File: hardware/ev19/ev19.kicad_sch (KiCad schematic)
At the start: 164 parts, among them CN1 Conn_05x02_Female, J1 USB_C_Receptacle, J11 Conn_02x05_Counter_Clockwise, J13 USB_C_Receptacle_USB2.0_16P, J2 Conn_01x02_Socket, J4 Conn_02x03_Odd_Even, J5 Conn_02x03_Odd_Even, J6 Conn_02x05_Counter_Clockwise, J7 Conn_02x05_Counter_Clockwise, J8 Conn_02x05_Counter_Clockwise, J9 Conn_02x05_Counter_Clockwise, Q1 2N7002, Q2 2N7002, Q3 2N7002, Q4 2N7002, SW1 SW_SPDT, SW2 SW_Push, SW3 SW_Push, U1 BQ21040DBV, U12 XC6227C301MR-G, U2 USBLC6-2P6, U3 STM32F072CBTx, U4 CH340C, U5 TPS63060, U7 ESP32-S3-WROOM-1, U9 TPS2116DRL, Y1 Crystal_GND24

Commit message: wip- laid out the analog power section, added screen cut outs, decided on positions
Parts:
- removed H5: MountingHole, MountingHole:MountingHole_2.7mm_M2.5, symbol Mechanical:MountingHole
- removed J13: USB_C_Receptacle_USB2.0_16P, Connector_USB:USB_C_Receptacle_HRO_TYPE-C-31-M-12, symbol Connector:USB_C_Receptacle_USB2.0_16P
- added J10: USB_C_Receptacle, Connector_USB:USB_C_Receptacle_HRO_TYPE-C-31-M-12, symbol Connector:USB_C_Receptacle_USB2.0_16P
- JP1: footprint Jumper:SolderJumper-3_P1.3mm_Bridged12_RoundedPad1.0x1.5mm -> (none)
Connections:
- net UI_SCL1: no longer R16.2
- net UI_SDA1: no longer R19.2
- net +3.3V_ES8311 renamed +3.3V_WM8960
- net ES8311_Sense renamed WM8960_Sense
- new net: J10.A1 (GND), J10.A12 (GND), J10.B1 (GND), J10.B12 (GND)
- new net: J10.A4 (VBUS), J10.A9 (VBUS), J10.B4 (VBUS), J10.B9 (VBUS)
- new net I2C1_SCL: R19.2
- new net I2C1_SDA: R16.2
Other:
- note removed: "7.071"
- moved on the sheet: C10, C11, C18, C7, JP3, NT1, R2, R52, U12

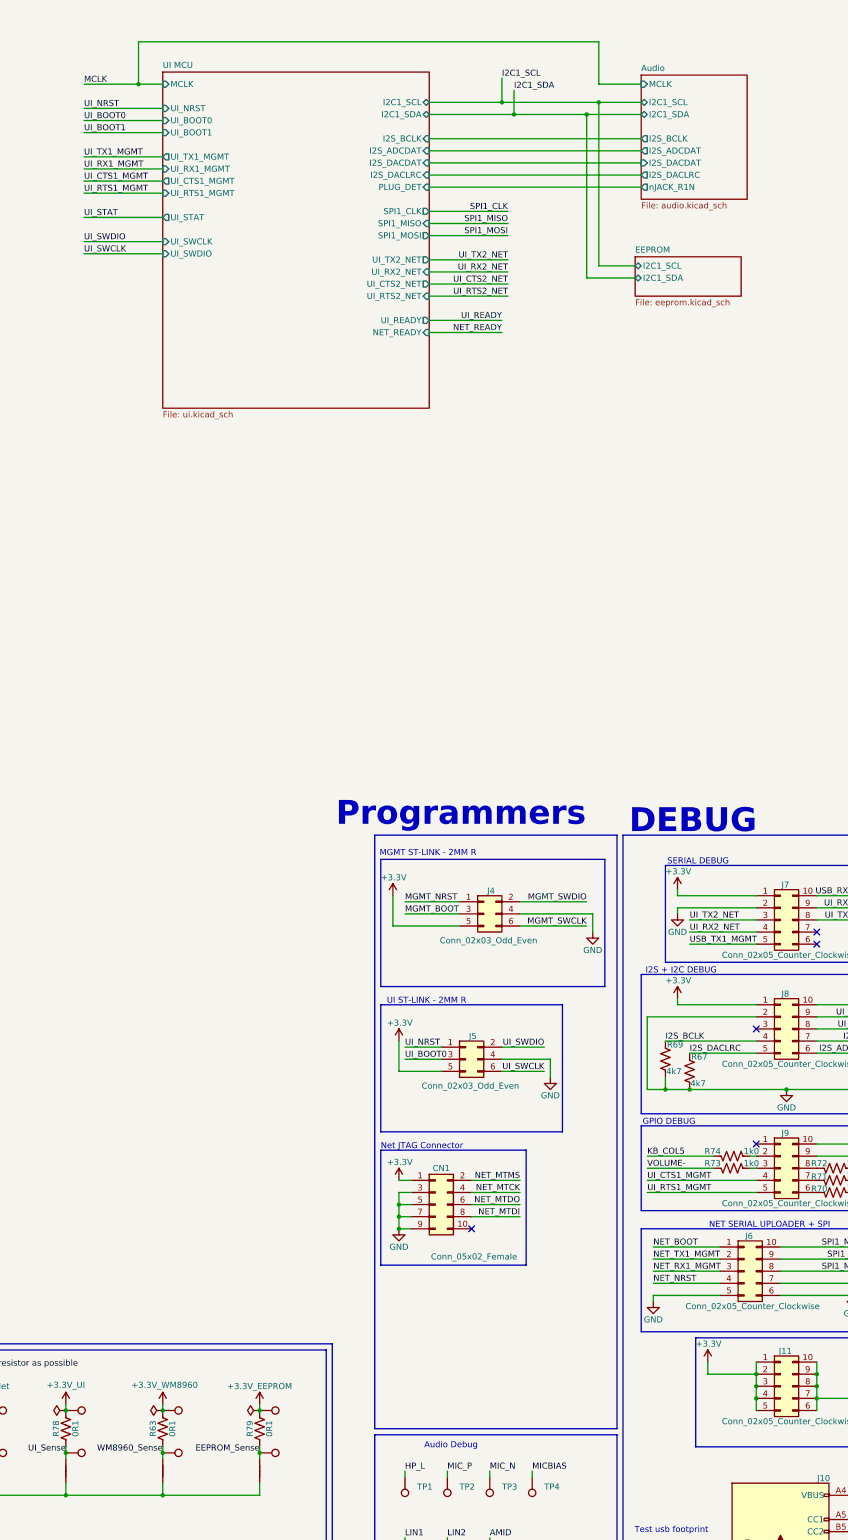
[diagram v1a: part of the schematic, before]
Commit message: Laid out all high speed lines, created gnda, 3.0va, and dgnd 3.3vd in analog sections
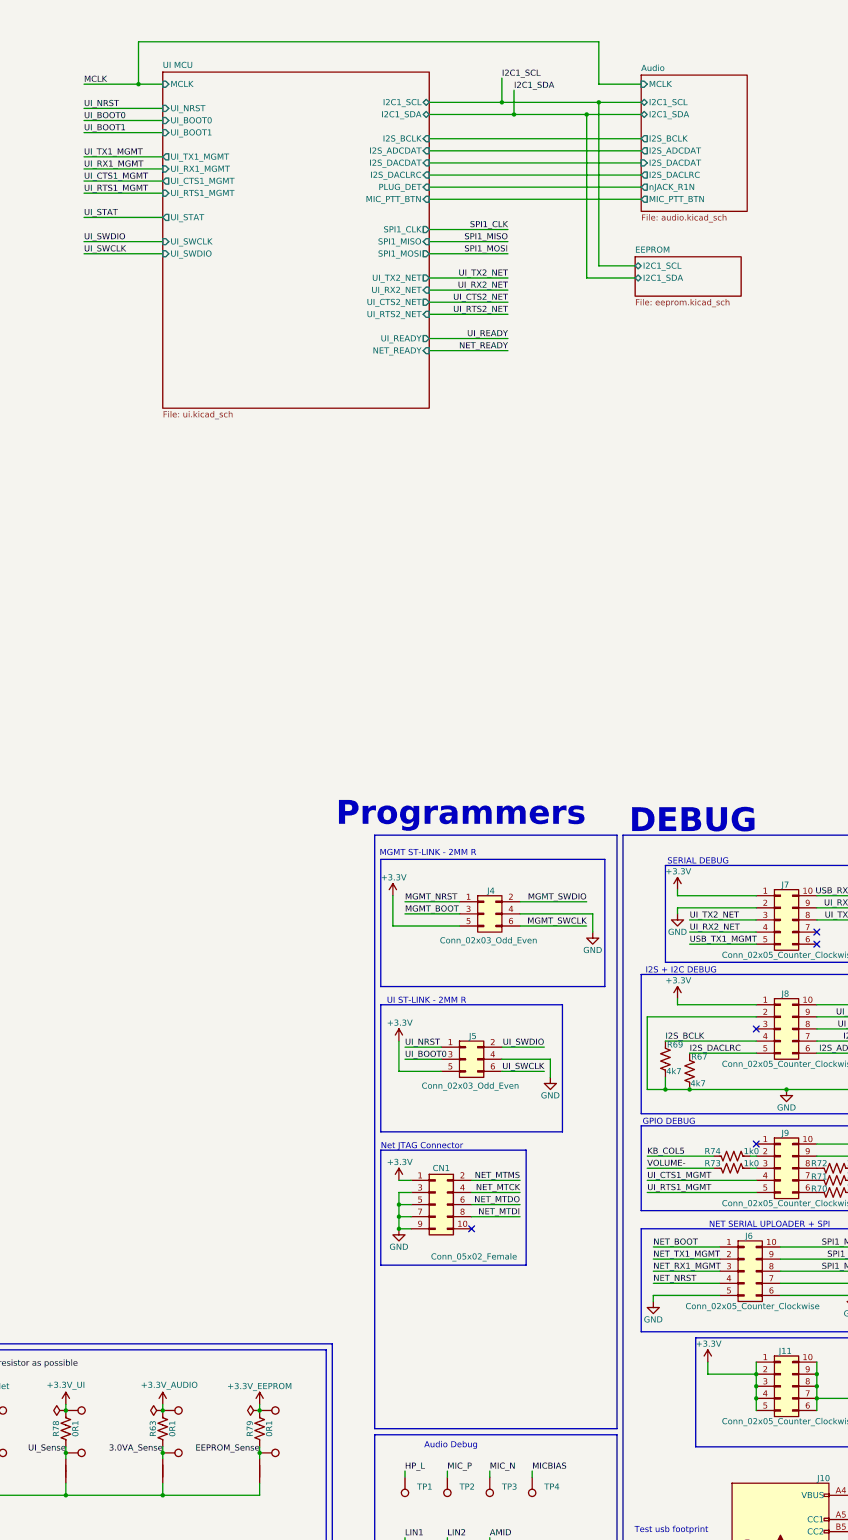
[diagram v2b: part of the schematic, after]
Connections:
- net +3.3V_WM8960 renamed +3.3V_AUDIO
- net WM8960_Sense renamed 3.0VA_Sense
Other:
- sheet Audio ports: added MIC_PTT_BTN; removed none
- sheet UI MCU ports: added MIC_PTT_BTN; removed none
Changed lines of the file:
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@@
 	(wire
 		(pts
-			(xy 482.6 63.5) (xy 466.09 63.5)
+			(xy 482.6 67.31) (xy 466.09 67.31)
 		)
 		(stroke
@@
 	(wire
 		(pts
-			(xy 482.6 60.96) (xy 466.09 60.96)
+			(xy 482.6 64.77) (xy 466.09 64.77)
 		)
 		(stroke
@@
 	(wire
 		(pts
-			(xy 466.09 83.82) (xy 481.33 83.82)
+			(xy 466.09 87.63) (xy 482.6 87.63)
 		)
 		(stroke
@@
 	(wire
 		(pts
-			(xy 466.09 73.66) (xy 482.6 73.66)
+			(xy 466.09 77.47) (xy 482.6 77.47)
 		)
 		(stroke
@@
 	(wire
 		(pts
-			(xy 466.09 78.74) (xy 482.6 78.74)
+			(xy 466.09 82.55) (xy 482.6 82.55)
 		)
 		(stroke
@@
 	(wire
 		(pts
-			(xy 466.09 76.2) (xy 482.6 76.2)
+			(xy 466.09 80.01) (xy 482.6 80.01)
 		)
 		(stroke
@@
 	(wire
 		(pts
-			(xy 466.09 71.12) (xy 482.6 71.12)
+			(xy 466.09 74.93) (xy 482.6 74.93)
 		)
 		(stroke
@@
 	(wire
 		(pts
+			(xy 466.09 58.42) (xy 510.54 58.42)
+		)
+		(stroke
+			(width 0)
+			(type default)
+		)
+	)
+	(wire
+		(pts
 			(xy 199.39 342.9) (xy 199.39 341.63)
 		)
@@
 	(wire
 		(pts
-			(xy 466.09 86.36) (xy 481.33 86.36)
+			(xy 466.09 90.17) (xy 482.6 90.17)
 		)
 		(stroke
@@
 	(wire
 		(pts
-			(xy 482.6 66.04) (xy 466.09 66.04)
+			(xy 482.6 69.85) (xy 466.09 69.85)
 		)
 		(stroke
@@
 	)
 	(label "UI_RTS2_NET"
-		(at 482.6 78.74 180)
+		(at 482.6 82.55 180)
 		(effects
 			(font
@@
 	)
 	(label "SPI1_CLK"
-		(at 482.6 60.96 180)
+		(at 482.6 64.77 180)
 		(effects
 			(font
@@
 	)
 	(label "UI_CTS2_NET"
-		(at 482.6 76.2 180)
+		(at 482.6 80.01 180)
 		(effects
 			(font
@@
 	)
 	(label "SPI1_MISO"
-		(at 482.6 63.5 180)
+		(at 482.6 67.31 180)
 		(effects
 			(font
@@
 	)
 	(label "UI_RX2_NET"
-		(at 482.6 73.66 180)
+		(at 482.6 77.47 180)
 		(effects
 			(font
@@
 	)
 	(label "NET_READY"
-		(at 481.33 86.36 180)
+		(at 482.6 90.17 180)
 		(effects
 			(font
@@
 		)
 	)
-	(label "WM8960_Sense"
+	(label "3.0VA_Sense"
 		(at 410.21 321.31 180)
 		(effects
@@
 	)
 	(label "UI_READY"
-		(at 481.33 83.82 180)
+		(at 482.6 87.63 180)
 		(effects
 			(font
@@
 	)
 	(label "UI_TX2_NET"
-		(at 482.6 71.12 180)
+		(at 482.6 74.93 180)
 		(effects
 			(font
@@
 	)
 	(label "SPI1_MOSI"
-		(at 482.6 66.04 180)
+		(at 482.6 69.85 180)
 		(effects
 			(font
@@
 			)
 		)
-		(property "Value" "+3.3V_WM8960"
+		(property "Value" "+3.3V_AUDIO"
 			(at 417.576 307.086 0)
 			(show_name no)
@@
 		)
 		(pin "NET_READY" input
-			(at 466.09 86.36 0)
+			(at 466.09 90.17 0)
 			(effects
 				(font
@@
 		)
 		(pin "SPI1_CLK" output
-			(at 466.09 60.96 0)
+			(at 466.09 64.77 0)
 			(effects
 				(font
@@
 		)
 		(pin "SPI1_MOSI" output
-			(at 466.09 66.04 0)
+			(at 466.09 69.85 0)
 			(effects
 				(font
@@
 		)
 		(pin "UI_CTS2_NET" output
-			(at 466.09 76.2 0)
+			(at 466.09 80.01 0)
 			(effects
 				(font
@@
 		)
 		(pin "UI_READY" output
-			(at 466.09 83.82 0)
+			(at 466.09 87.63 0)
 			(effects
 				(font
@@
 		)
 		(pin "UI_RTS2_NET" input
-			(at 466.09 78.74 0)
+			(at 466.09 82.55 0)
 			(effects
 				(font
@@
 		)
 		(pin "UI_RX2_NET" input
-			(at 466.09 73.66 0)
+			(at 466.09 77.47 0)
 			(effects
 				(font
@@
 		)
 		(pin "UI_TX2_NET" output
-			(at 466.09 71.12 0)
+			(at 466.09 74.93 0)
 			(effects
 				(font
@@
 		)
 		(pin "SPI1_MISO" input
-			(at 466.09 63.5 0)
+			(at 466.09 67.31 0)
 			(effects
 				(font
@@
 			)
 		)
+		(pin "MIC_PTT_BTN" input
+			(at 466.09 58.42 0)
+			(effects
+				(font
+					(size 1.27 1.27)
+				)
+				(justify right)
+			)
+		)
 		(instances
 			(project "ev19"
@@
 	(sheet
 		(at 510.54 32.385)
-		(size 22.225 26.035)
+		(size 22.225 28.575)
 		(exclude_from_sim no)
 		(in_bom yes)
@@
 		)
 		(property "Sheetfile" "audio.kicad_sch"
-			(at 510.54 59.0046 0)
+			(at 510.54 61.5446 0)
 			(show_name no)
 			(do_not_autoplace no)
@@
 			(effects
 				(font
+					(size 1.27 1.27)
+				)
+				(justify left)
+			)
+		)
+		(pin "MIC_PTT_BTN" output
+			(at 510.54 58.42 180)
+			(effects
+				(font

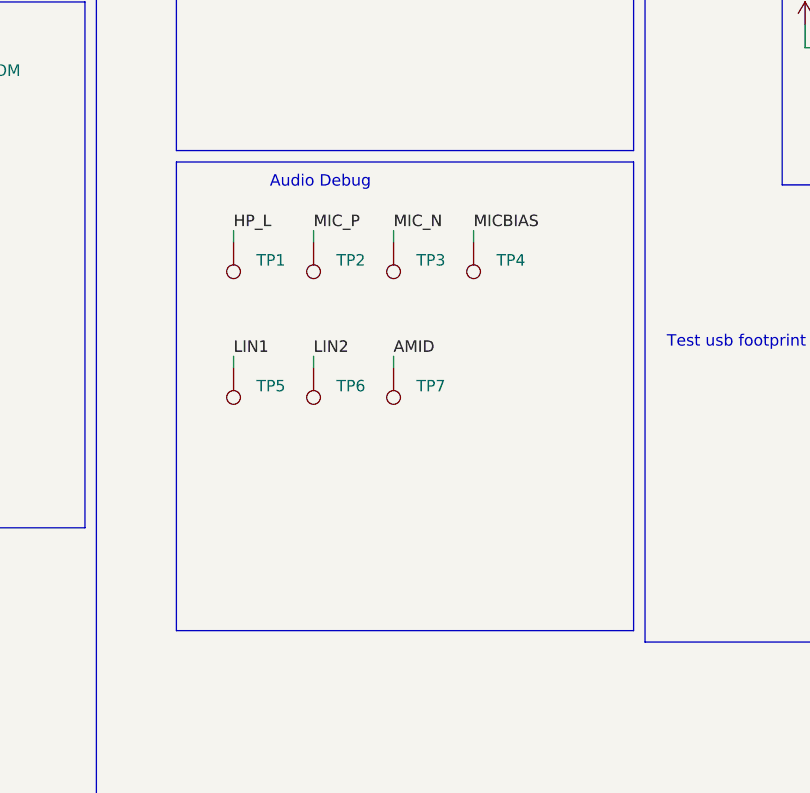
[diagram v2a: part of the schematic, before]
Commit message: Fixed ES8311 symbol, pins were wrong. Laid out audio section. Routed many non-high speed traces
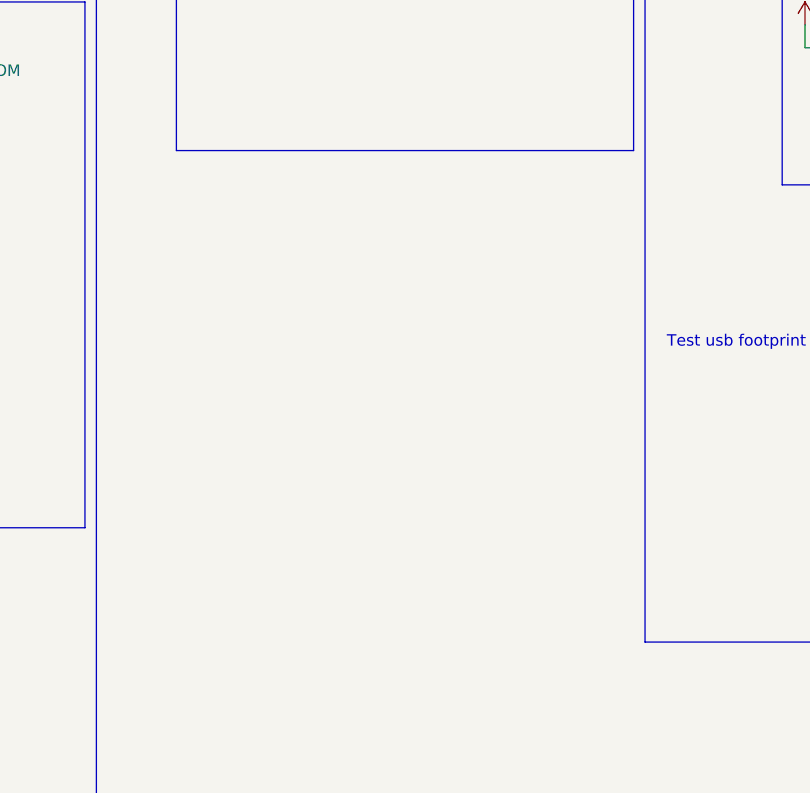
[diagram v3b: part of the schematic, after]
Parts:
- removed TP1, TP2, TP3, TP4, TP5, TP6, TP7: TestPoint, TestPoint:TestPoint_THTPad_D2.0mm_Drill1.0mm, symbol Connector:TestPoint
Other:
- note removed: "Audio Debug"

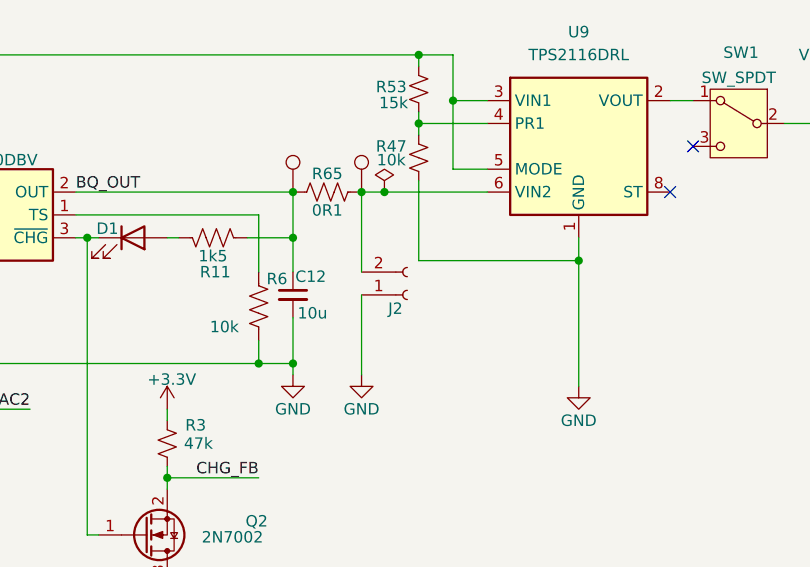
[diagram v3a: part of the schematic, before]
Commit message: Redesigned digital section again to fit the battery better. Chose where the screen connector and battery connector go
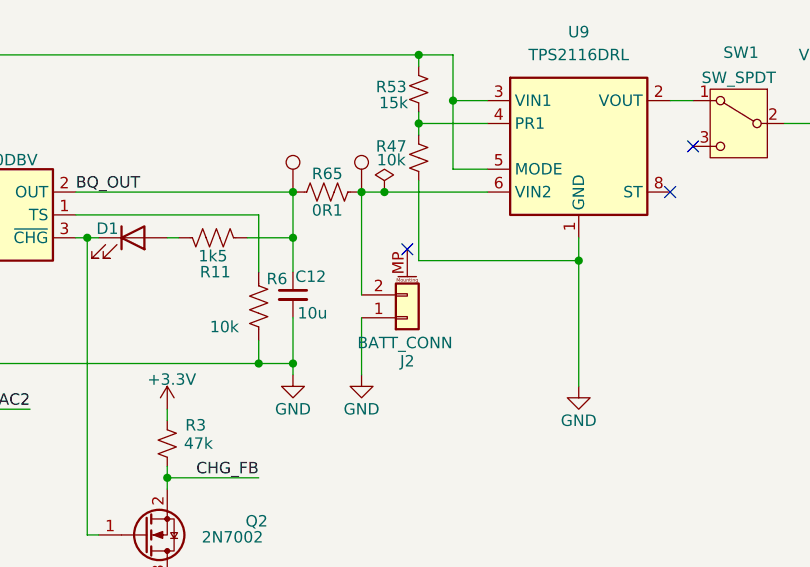
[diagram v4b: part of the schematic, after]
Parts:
- removed J2: Conn_01x02_Socket, Hactar_Footprints:JST_PH_S2B-PH-SM4-TB_1x02-1MP_P2.00mm_Horizontal, symbol Connector:Conn_01x02_Socket
- added J2: BATT_CONN, Connector_JST:JST_PH_S2B-PH-SM4-TB_1x02-1MP_P2.00mm_Horizontal, symbol Connector_Generic_MountingPin:Conn_01x02_MountingPin
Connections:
- net GND: now also J2.1 (Pin_1)
- net at R65.2, TP32.1, U9.6 (VIN2): now also J2.2 (Pin_2)
- no-connect marks 41 -> 42
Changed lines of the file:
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@@
 	)
 	(no_connect
+		(at 92.71 342.9)
+	)
+	(no_connect
 		(at 532.13 368.3)
 	)
@@
 	(wire
 		(pts
-			(xy 87.63 347.98) (xy 87.63 356.87)
+			(xy 87.63 350.52) (xy 87.63 356.87)
 		)
 		(stroke
@@
 	(wire
 		(pts
-			(xy 87.63 336.55) (xy 87.63 345.44)
+			(xy 87.63 336.55) (xy 87.63 347.98)
 		)
 		(stroke
@@
 	)
 	(symbol
+		(lib_id "Connector_Generic_MountingPin:Conn_01x02_MountingPin")
+		(at 92.71 350.52 0)
+		(mirror x)
+		(unit 1)
+		(body_style 1)
+		(exclude_from_sim no)
+		(in_bom yes)
+		(on_board yes)
+		(in_pos_files yes)
+		(dnp no)
+		(property "Reference" "J2"
+			(at 92.71 355.346 0)
+			(show_name no)
+			(do_not_autoplace no)
+			(effects
+				(font
+					(size 1.27 1.27)
+				)
+			)
+		)
+		(property "Value" "BATT_CONN"
+			(at 92.456 353.314 0)
+			(show_name no)
+			(do_not_autoplace no)
+			(effects
+				(font
+					(size 1.27 1.27)
+				)
+			)
+		)
+		(property "Footprint" "Connector_JST:JST_PH_S2B-PH-SM4-TB_1x02-1MP_P2.00mm_Horizontal"
+			(at 92.71 350.52 0)
+			(hide yes)
+			(show_name no)
+			(do_not_autoplace no)
+			(effects
+				(font
+					(size 1.27 1.27)
+				)
+			)
+		)
+		(property "Datasheet" ""
+			(at 92.71 350.52 0)
+			(hide yes)
+			(show_name no)
+			(do_not_autoplace no)
+			(effects
+				(font
+					(size 1.27 1.27)
+				)
+			)
+		)
+		(property "Description" "Generic connectable mounting pin connector, single row, 01x02, script generated (kicad-library-utils/schlib/autogen/connector/)"
+			(at 92.71 350.52 0)
+			(hide yes)
+			(show_name no)
+			(do_not_autoplace no)
+			(effects
+				(font
+					(size 1.27 1.27)
+				)
+			)
+		)
+		(property "JLCPCB Part #" "C295747"
+			(at 92.71 350.52 0)
+			(hide yes)
+			(show_name no)
+			(do_not_autoplace no)
+			(effects
+				(font
+					(size 1.27 1.27)
+				)
+			)
+		)
+		(pin "1"
+		)
+		(pin "2"
+		)
+		(pin "MP"
+		)
+		(instances
+			(project "ev19"
+				(path "/bd865368-262b-4f76-b7a6-1673c2cb0f8c"
+					(reference "J2")
+					(unit 1)
+				)
+			)
+		)
+	)
+	(symbol
 		(lib_id "Device:C_Small")
 		(at 187.96 345.44 0)
@@
 					(unit 1)
 				)
-			)
-		)
-	)
-	(symbol
-		(lib_id "Connector:Conn_01x02_Socket")
-		(at 92.71 347.98 0)
-		(mirror x)
-		(unit 1)
-		(body_style 1)
-		(exclude_from_sim no)
-		(in_bom yes)
-		(on_board yes)
-		(in_pos_files yes)
-		(dnp no)
-		(property "Reference" "J2"
-			(at 92.202 349.504 0)
-			(show_name no)
-			(do_not_autoplace no)
-			(effects
-				(font
-					(size 1.27 1.27)
-				)
-				(justify right)
-			)
-		)
-		(property "Value" "Conn_01x02_Socket"
-			(at 96.52 354.33 90)
-			(hide yes)
-			(show_name no)
-			(do_not_autoplace no)
-			(effects
-				(font
-					(size 1.27 1.27)
-				)
-				(justify right)
-			)
-		)
-		(property "Footprint" "Hactar_Footprints:JST_PH_S2B-PH-SM4-TB_1x02-1MP_P2.00mm_Horizontal"
-			(at 92.71 347.98 0)
-			(hide yes)
-			(show_name no)
-			(do_not_autoplace no)
-			(effects
-				(font
-					(size 1.27 1.27)
-				)
-			)
-		)
-		(property "Datasheet" ""
-			(at 92.71 347.98 0)
-			(hide yes)
-			(show_name no)
-			(do_not_autoplace no)
-			(effects
-				(font
-					(size 1.27 1.27)
-				)
-			)
-		)
-		(property "Description" "Generic connector, single row, 01x02, script generated"
-			(at 92.71 347.98 0)
-			(hide yes)
-			(show_name no)
-			(do_not_autoplace no)
-			(effects
-				(font
-					(size 1.27 1.27)
-				)
-			)
-		)
-		(property "JLCPCB Part #" "C295747"
-			(at 92.71 347.98 0)
-			(hide yes)
-			(show_name no)
-			(do_not_autoplace no)
-			(effects
-				(font
-					(size 1.27 1.27)
-				)
-			)
-		)
-		(property "FT Rotation Offset" "180"
-			(at 92.71 347.98 90)
-			(hide yes)
-			(show_name no)
-			(do_not_autoplace no)
-			(effects
-				(font
-					(size 1.27 1.27)
-				)
-			)
-		)
-		(property "Availability" ""
-			(at 92.71 347.98 0)
-			(show_name no)
-			(do_not_autoplace no)
-			(effects
-				(font
-					(size 1.27 1.27)
-				)
-			)
-		)
-		(property "Sim.Device" ""
-			(at 92.71 347.98 0)
-			(show_name no)
-			(do_not_autoplace no)
-			(effects
-				(font
-					(size 1.27 1.27)
-				)
-			)
-		)
-		(property "JLCPCB Position Offset" ""
-			(at 92.71 347.98 0)
-			(hide yes)
-			(show_name no)
-			(do_not_autoplace no)
-			(effects
-				(font
-					(size 1.27 1.27)
-				)
-			)
-		)
-		(property "Sim.Type" ""
-			(at 92.71 347.98 0)
-			(hide yes)
-			(show_name no)
-			(do_not_autoplace no)
-			(effects
-				(font
-					(size 1.27 1.27)
-				)
-			)
-		)
-		(pin "1"
-		)
-		(pin "2"
-		)
-		(instances
-			(project "ev19"
-				(path "/bd865368-262b-4f76-b7a6-1673c2cb0f8c"
-					(reference "J2")
-					(unit 1)
-				)
-			)
-			(project "Buckboost converter"
-				(path "/e24f98db-dd9d-44b5-9774-c601a7625859"
-					(reference "J3")
-					(unit 1)
-				)
